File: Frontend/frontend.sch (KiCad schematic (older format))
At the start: 0 parts

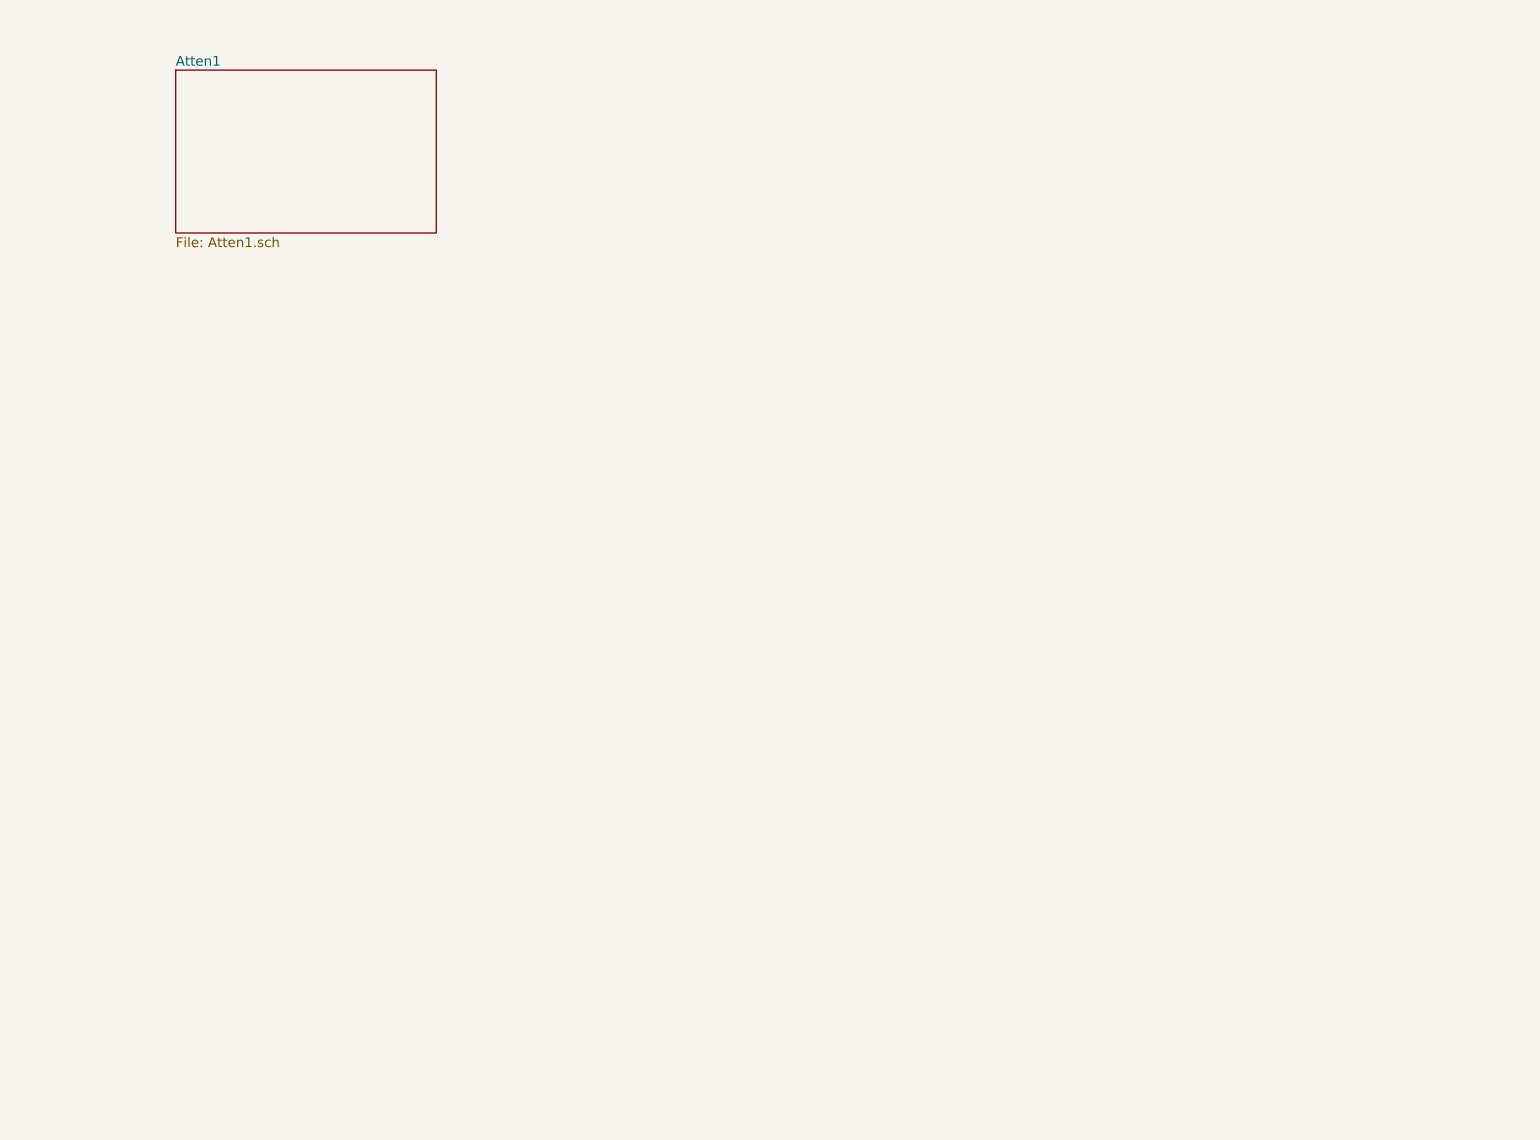
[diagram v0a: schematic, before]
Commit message: Frontend schematic ready to go to layout
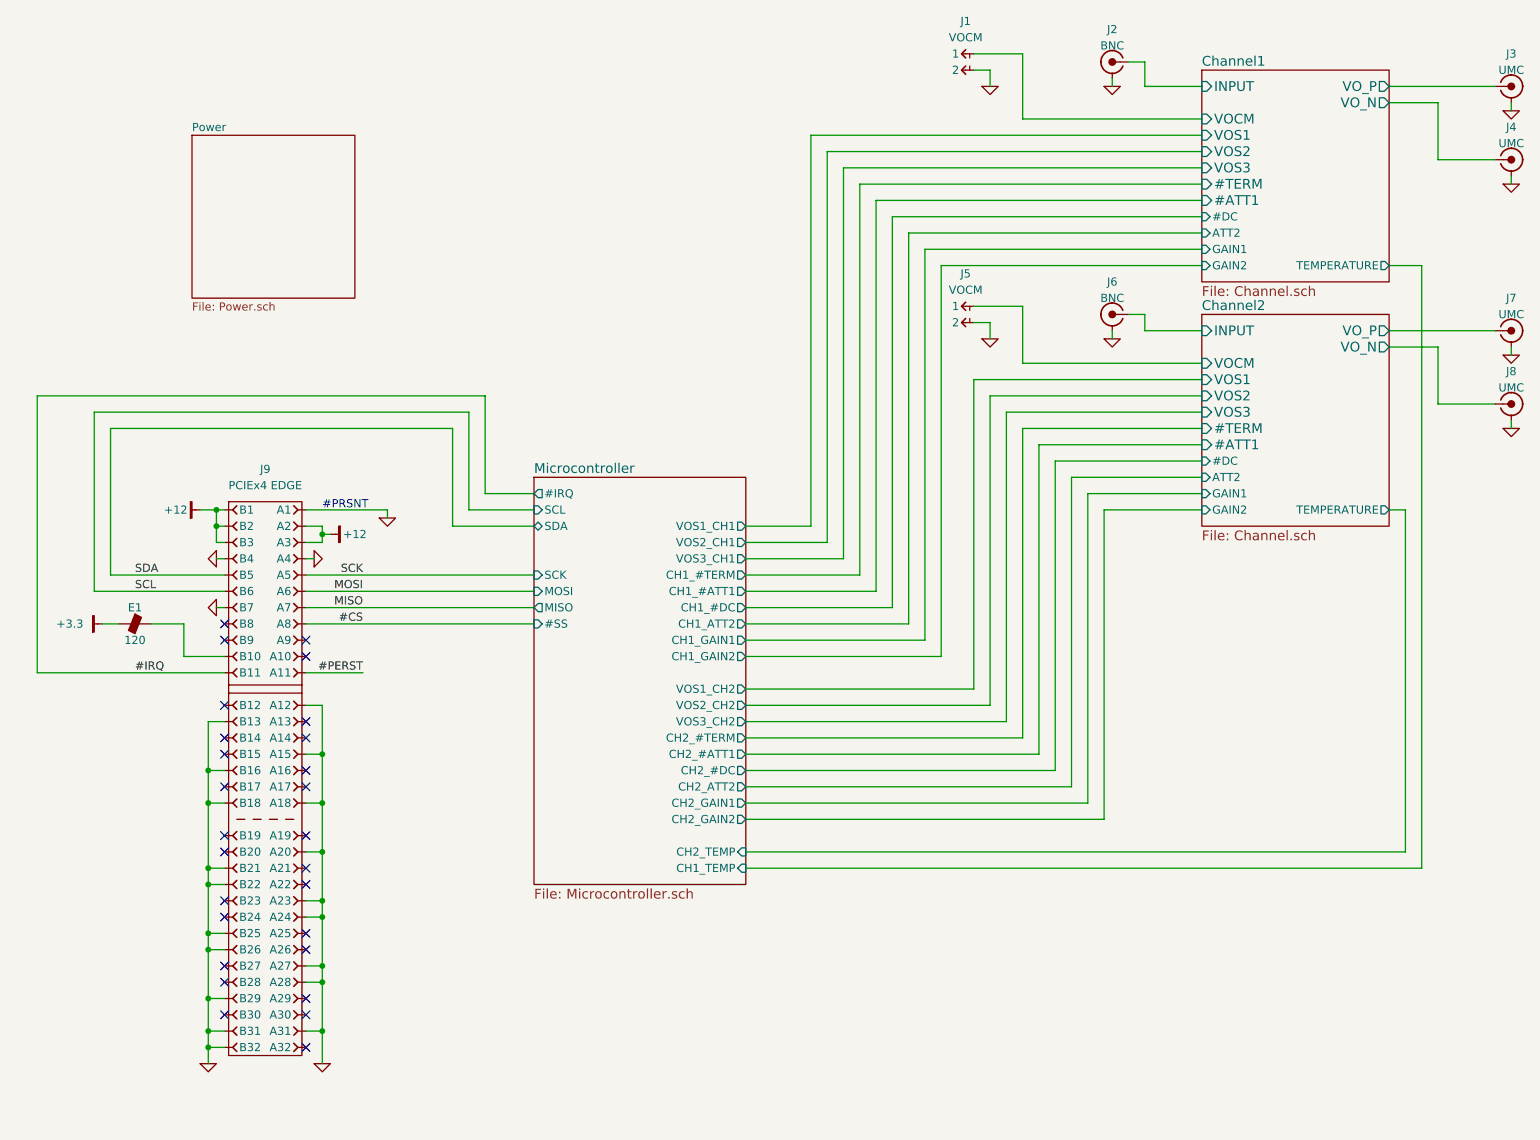
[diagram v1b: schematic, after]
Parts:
- added E1: 120, IPC7351-Nominal:RESC3216X60, symbol BEAD-1206
- added J1, J5: VOCM, conn-100mil:CONN-100MIL-M-1x2, symbol CONN-100MIL-M-1x2
- added J2, J6: BNC, manuf:CONN-BNC-1-1337543-0, symbol CONN-TE-1-1337543-0
- added J3, J4, J7, J8: UMC, conn-molex:CONN-MOLEX-0734120110, symbol CONN-MOLEX-0734120110
- added J9: PCIEx4 EDGE, conn-fci:CONN-10018784-10201TLF-PCIEx4-FCI, symbol CONN-10018784-10201TLF-PCIEx4
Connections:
- new net: E1.2, J9.B10
- new net #CS: J9.A8
- new net #IRQ: J9.B11
- new net #PERST: J9.A11
- new net +12: J9.A2, J9.A3, J9.B1, J9.B2, J9.B3
- new net +3.3: E1.1
- new net Channel1/INPUT: J2.1
- new net Channel1/VOCM: J1.1
- new net Channel1/VO_N: J4.1
- new net Channel1/VO_P: J3.1
- new net Channel2/INPUT: J6.1
- new net Channel2/VOCM: J5.1
- new net Channel2/VO_N: J8.1
- new net Channel2/VO_P: J7.1
- new net GND: J1.2, J2.2, J3.2, J4.2, J5.2, J6.2, J7.2, J8.2, J9.A1, J9.A12, J9.A15, J9.A18, J9.A20, J9.A23, J9.A24, J9.A27, J9.A28, J9.A31, J9.A4, J9.B13, J9.B16, J9.B18, J9.B21, J9.B22, J9.B25, J9.B26, J9.B29, J9.B31, J9.B32, J9.B4, J9.B7
- new net MISO: J9.A7
- new net MOSI: J9.A6
- new net SCK: J9.A5
- new net SCL: J9.B6
- new net SDA: J9.B5
- no-connect marks 0 -> 27
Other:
- note added: "#PRSNT"

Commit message: More layout work
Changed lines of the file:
@@
 F7 "CH2_#TERM" O R 5100 5300 50
 F8 "CH2_#ATT1" O R 5100 5400 50
-F9 "SDA" B L 3800 4000 50
-F10 "SCL" I L 3800 3900 50
+F9 "SDA" B L 3800 4200 50
+F10 "SCL" I L 3800 4100 50
 F11 "#SS" I L 3800 4600 50
-F12 "#IRQ" O L 3800 3800 50
+F12 "#IRQ" O L 3800 4000 50
 F13 "CH2_#DC" O R 5100 5500 50
 F14 "CH1_#DC" O R 5100 4500 50
@@
 F27 "CH1_TEMP" I R 5100 6100 50
 F28 "CH2_TEMP" I R 5100 6000 50
+F29 "TEMP_VRELAY" I L 3800 3800 50
+F30 "TEMP_V5" I L 3800 3900 50
 $EndSheet
 $Sheet
@@
 F0 "Power" 50
 F1 "Power.sch" 50
+F2 "TEMP_VRELAY" O R 2700 1700 50
+F3 "TEMP_V5" O R 2700 1800 50
 $EndSheet
 $Comp
@@
 Connection ~ 2500 5400
 Wire Wire Line
-	3800 4000 3300 4000
-Wire Wire Line
-	3300 4000 3300 3400
-Wire Wire Line
-	3300 3400 1200 3400
+	3800 4200 3000 4200
+Wire Wire Line
+	3000 4200 3000 3400
+Wire Wire Line
+	3000 3400 1200 3400
 Wire Wire Line
 	1200 3400 1200 4300
@@
 	1100 4400 1100 3300
 Wire Wire Line
-	1100 3300 3400 3300
-Wire Wire Line
-	3400 3300 3400 3900
-Wire Wire Line
-	3400 3900 3800 3900
+	1100 3300 3100 3300
+Wire Wire Line
+	3100 3300 3100 4100
+Wire Wire Line
+	3100 4100 3800 4100
 Wire Wire Line
 	1250 4600 1150 4600
@@
 	1650 4800 1900 4800
 Wire Wire Line
-	3800 3800 3500 3800
-Wire Wire Line
-	3500 3800 3500 3200
-Wire Wire Line
-	3500 3200 750  3200
+	3800 4000 3200 4000
+Wire Wire Line
+	3200 4000 3200 3200
+Wire Wire Line
+	3200 3200 750  3200
 Wire Wire Line
 	750  3200 750  4900
@@
 Wire Wire Line
 	9250 2400 9050 2400
+Wire Wire Line
+	3800 3900 3400 3900
+Wire Wire Line
+	3400 3900 3400 1800
+Wire Wire Line
+	3400 1800 2700 1800
+Wire Wire Line
+	2700 1700 3500 1700
+Wire Wire Line
+	3500 1700 3500 3800
+Wire Wire Line
+	3500 3800 3800 3800
 $EndSCHEMATC

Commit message: Schematic touchups
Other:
- moved on the sheet: E1

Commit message: Route #IRQ and #PERST
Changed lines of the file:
@@
 LIBS:Altera
 LIBS:conn-te
+LIBS:Vishay
+LIBS:semi-trans-OnSemi
 LIBS:frontend-cache
 EELAYER 25 0
@@
 F29 "TEMP_VRELAY" I L 3800 3800 50
 F30 "TEMP_V5" I L 3800 3900 50
+F31 "#PERST" I L 3800 4900 50
 $EndSheet
 $Sheet
@@
 	2400 4600 3800 4600
 Wire Wire Line
-	2750 4900 2400 4900
+	2400 4900 3800 4900
 Wire Wire Line
 	1900 5200 1800 5200

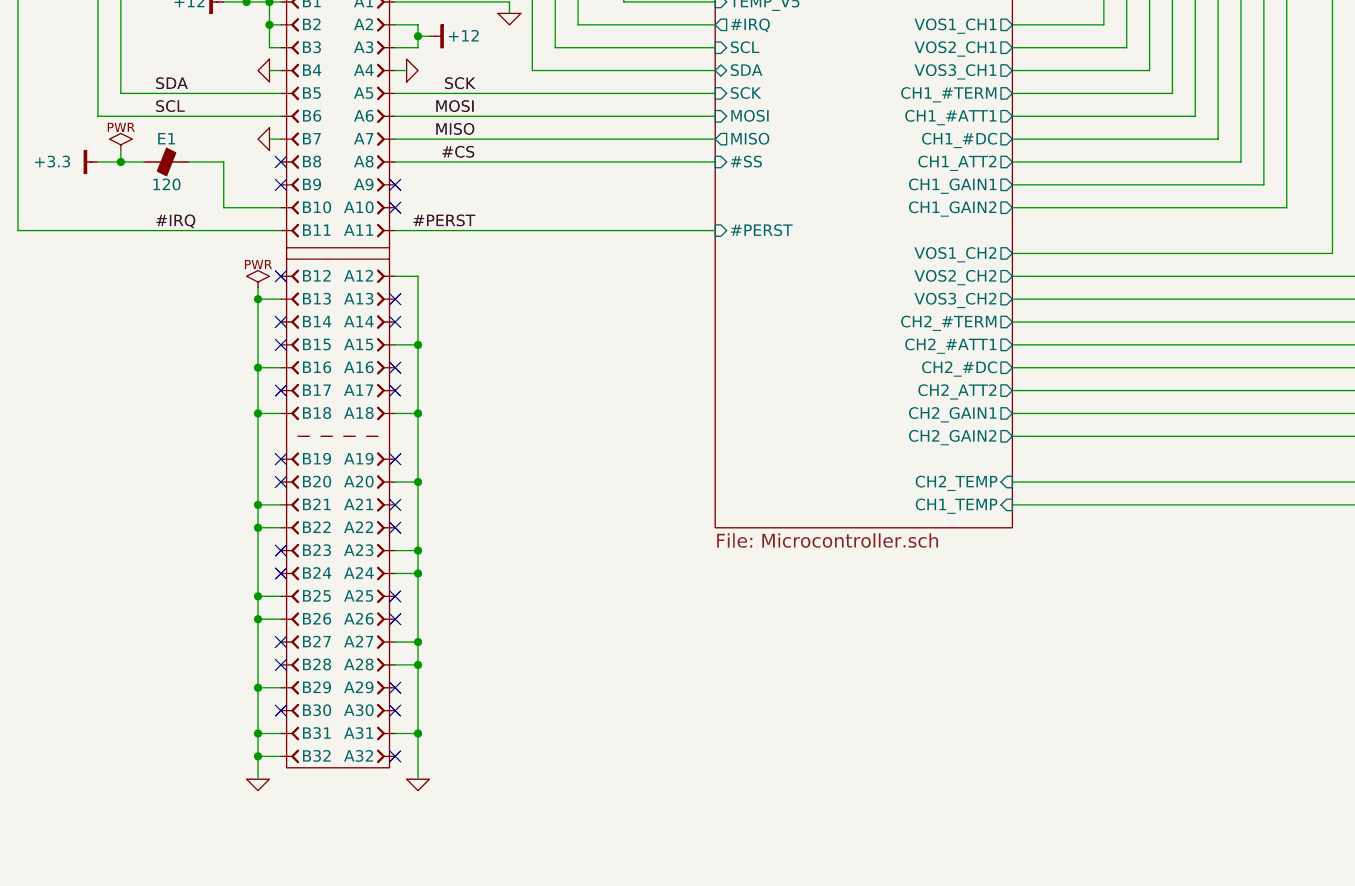
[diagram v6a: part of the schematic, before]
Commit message: Add testpoints
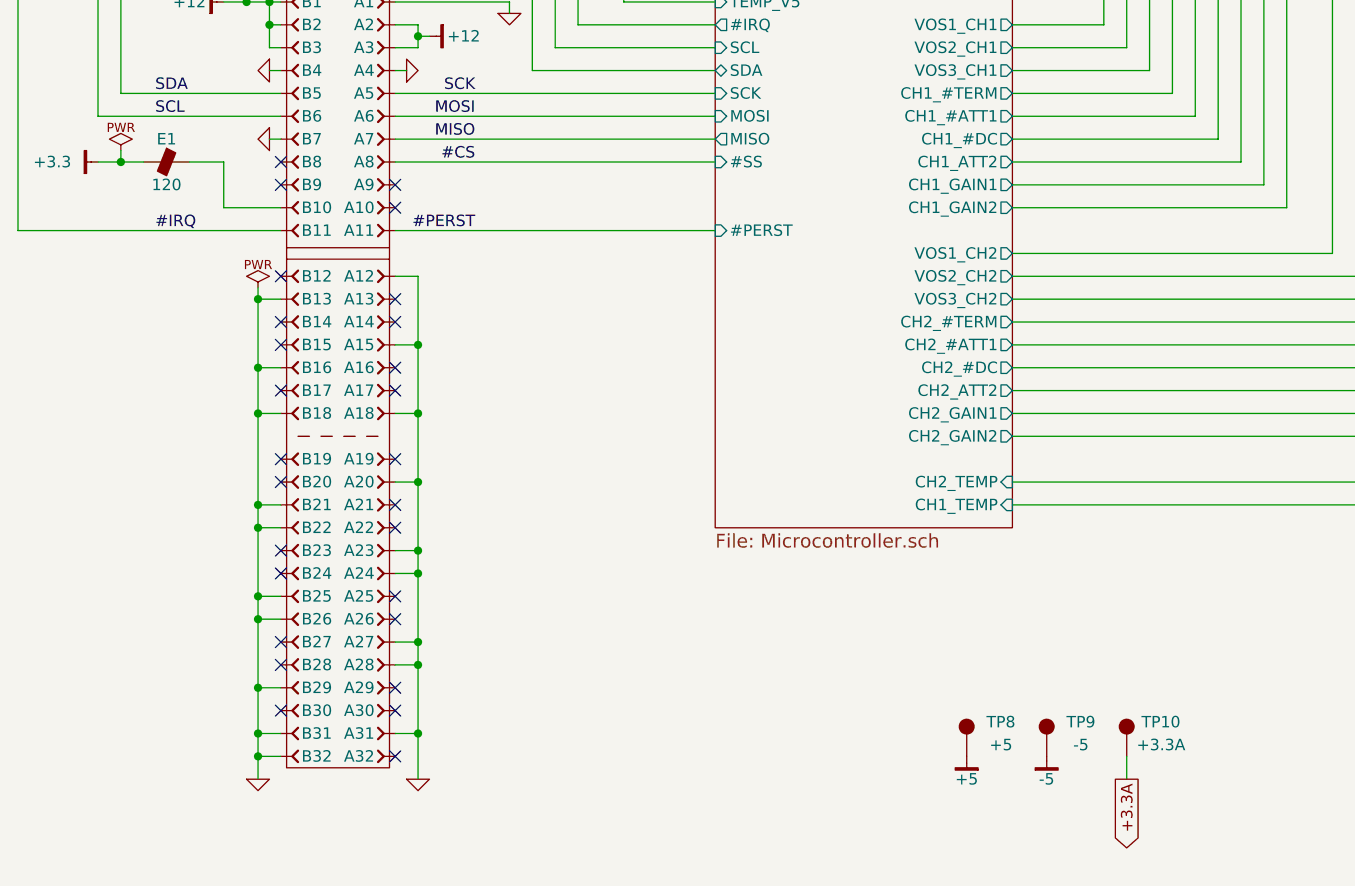
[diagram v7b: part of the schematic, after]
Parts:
- added TP10: +3.3A, conn-test:TEST-SMD-SMALL, symbol TESTPOINT
- added TP8: +5, conn-test:TEST-SMD-SMALL, symbol TESTPOINT
- added TP9: -5, conn-test:TEST-SMD-SMALL, symbol TESTPOINT
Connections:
- new net +3.3A: TP10.1
- new net +5: TP8.1
- new net -5: TP9.1
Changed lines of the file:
@@
 	3100 4100 3800 4100
 Wire Wire Line
-	1300 4600 1100 4600
+	1100 4600 1300 4600
 Wire Wire Line
 	1500 4600 1650 4600
@@
 $EndComp
 Connection ~ 1800 5200
+$Comp
+L TESTPOINT TP8
+U 1 1 5558DEAC
+P 4900 7200
+F 0 "TP8" H 5050 7350 50  0000 C CNN
+F 1 "+5" H 5050 7250 50  0000 C CNN
+F 2 "conn-test:TEST-SMD-SMALL" H 4900 7200 50  0001 C CNN
+F 3 "" H 4900 7200 50  0000 C CNN
+	1    4900 7200
+	1    0    0    -1
+$EndComp
+$Comp
+L +5 #PWR021
+U 1 1 5558E053
+P 4900 7200
+F 0 "#PWR021" H 4900 7250 30  0001 C CNN
+F 1 "+5" H 4900 7300 50  0000 C CNN
+F 2 "" H 4900 7200 60  0000 C CNN
+F 3 "" H 4900 7200 60  0000 C CNN
+	1    4900 7200
+	-1   0    0    1
+$EndComp
+$Comp
+L TESTPOINT TP9
+U 1 1 5558E378
+P 5250 7200
+F 0 "TP9" H 5400 7350 50  0000 C CNN
+F 1 "-5" H 5400 7250 50  0000 C CNN
+F 2 "conn-test:TEST-SMD-SMALL" H 5250 7200 50  0001 C CNN
+F 3 "" H 5250 7200 50  0000 C CNN
+	1    5250 7200
+	1    0    0    -1
+$EndComp
+$Comp
+L -5 #PWR022
+U 1 1 5558E5C7
+P 5250 7200
+F 0 "#PWR022" H 5250 7150 30  0001 C CNN
+F 1 "-5" H 5250 7100 50  0000 C CNN
+F 2 "" H 5250 7200 60  0000 C CNN
+F 3 "" H 5250 7200 60  0000 C CNN
+	1    5250 7200
+	1    0    0    -1
+$EndComp
+$Comp
+L TESTPOINT TP10
+U 1 1 5558E8F0
+P 5600 7200
+F 0 "TP10" H 5750 7350 50  0000 C CNN
+F 1 "+3.3A" H 5750 7250 50  0000 C CNN
+F 2 "conn-test:TEST-SMD-SMALL" H 5600 7200 50  0001 C CNN
+F 3 "" H 5600 7200 50  0000 C CNN
+	1    5600 7200
+	1    0    0    -1
+$EndComp
+Text GLabel 5600 7300 3    50   Output ~ 0
++3.3A
+Wire Wire Line
+	5600 7300 5600 7200
 $EndSCHEMATC

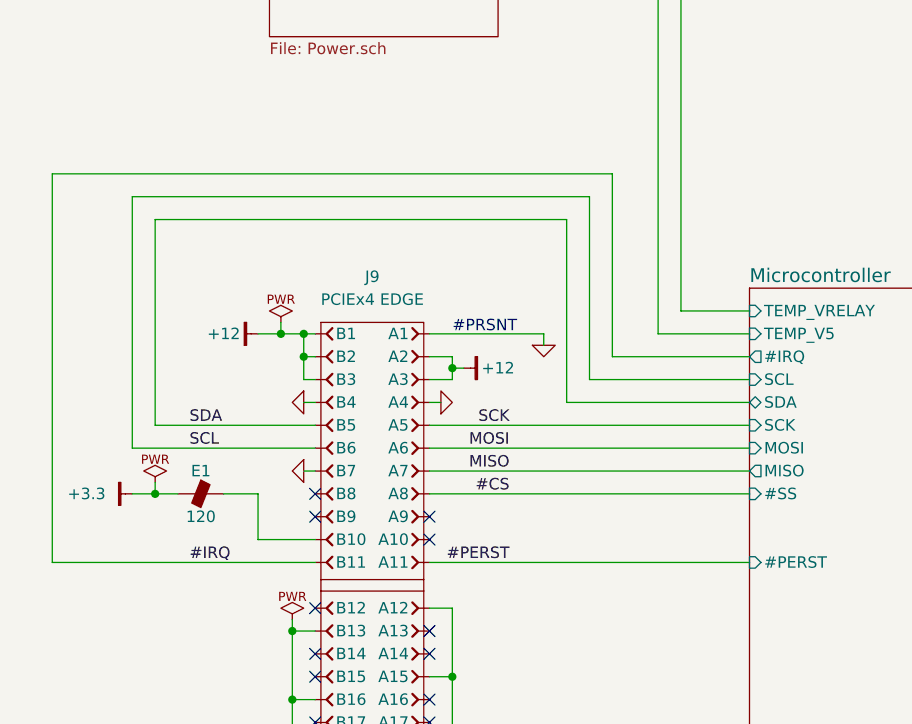
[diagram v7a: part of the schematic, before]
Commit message: Digital decoupling/termination tweaks
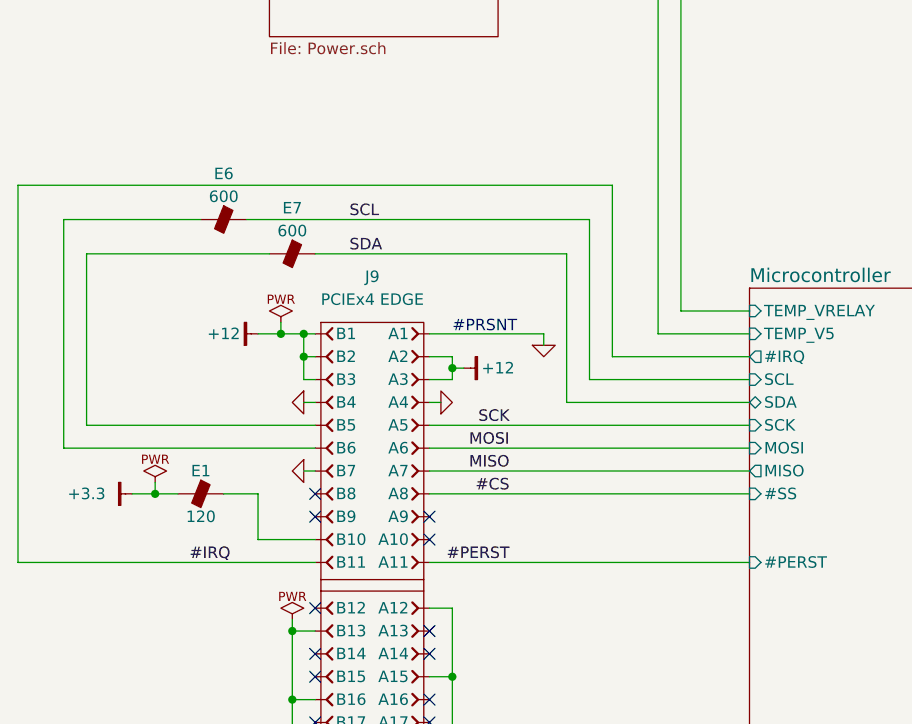
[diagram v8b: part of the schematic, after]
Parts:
- added E6, E7: 600, IPC7351-Nominal:INDC1005X60, symbol BEAD-0402
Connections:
- net SCL: now also E6.2; no longer J9.B6
- net SDA: now also E7.2; no longer J9.B5
- new net: E7.1, J9.B5
- new net: E6.1, J9.B6
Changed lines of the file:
@@
 	0    1    1    0
 $EndComp
-Text Label 1350 4400 0    50   ~ 0
+Text Label 2050 3400 0    50   ~ 0
 SCL
-Text Label 1350 4300 0    50   ~ 0
+Text Label 2050 3550 0    50   ~ 0
 SDA
 $Comp
@@
 	2450 4200 2400 4200
 Wire Wire Line
-	750  4900 1900 4900
+	600  4900 1900 4900
 Wire Wire Line
 	1850 4500 1900 4500
 Wire Wire Line
-	1100 4400 1900 4400
-Wire Wire Line
-	1200 4300 1900 4300
+	800  4400 1900 4400
+Wire Wire Line
+	900  4300 1900 4300
 Wire Wire Line
 	1850 4200 1900 4200
@@
 Connection ~ 2500 5400
 Wire Wire Line
-	3800 4200 3000 4200
-Wire Wire Line
-	3000 4200 3000 3400
-Wire Wire Line
-	3000 3400 1200 3400
-Wire Wire Line
-	1200 3400 1200 4300
-Wire Wire Line
-	1100 4400 1100 3300
-Wire Wire Line
-	1100 3300 3100 3300
-Wire Wire Line
-	3100 3300 3100 4100
+	3000 4200 3800 4200
+Wire Wire Line
+	3000 3550 3000 4200
+Wire Wire Line
+	900  3550 900  4300
+Wire Wire Line
+	800  4400 800  3400
+Wire Wire Line
+	3100 3400 3100 4100
 Wire Wire Line
 	3100 4100 3800 4100
@@
 	3800 4000 3200 4000
 Wire Wire Line
-	3200 4000 3200 3200
-Wire Wire Line
-	3200 3200 750  3200
-Wire Wire Line
-	750  3200 750  4900
+	3200 4000 3200 3250
+Wire Wire Line
+	3200 3250 600  3250
+Wire Wire Line
+	600  3250 600  4900
 Wire Wire Line
 	7450 1150 7550 1150
@@
 Wire Wire Line
 	5600 7300 5600 7200
+$Comp
+L BEAD-0402 E?
+U 1 1 555A74A2
+P 1500 3400
+AR Path="/552B011F/555A74A2" Ref="E?"  Part="1"
+AR Path="/555A74A2" Ref="E6"  Part="1"
+F 0 "E6" H 1500 3600 50  0000 C CNN
+F 1 "600" H 1500 3500 50  0000 C CNN
+F 2 "IPC7351-Nominal:INDC1005X60" H 1500 3400 50  0001 C CNN
+F 3 "" H 1500 3450 60  0000 C CNN
+F 4 "PE-0402FB601ST" H 1500 3400 60  0001 C CNN "PN"
+F 5 "Pulse" H 1500 3400 60  0001 C CNN "Manuf"
+F 6 "DIST DIGIKEY 553-2374-1-ND" H 1500 3400 60  0001 C CNN "BOM"
+	1    1500 3400
+	1    0    0    -1
+$EndComp
+$Comp
+L BEAD-0402 E?
+U 1 1 555A757C
+P 1800 3550
+AR Path="/552B011F/555A757C" Ref="E?"  Part="1"
+AR Path="/555A757C" Ref="E7"  Part="1"
+F 0 "E7" H 1800 3750 50  0000 C CNN
+F 1 "600" H 1800 3650 50  0000 C CNN
+F 2 "IPC7351-Nominal:INDC1005X60" H 1800 3550 50  0001 C CNN
+F 3 "" H 1800 3600 60  0000 C CNN
+F 4 "PE-0402FB601ST" H 1800 3550 60  0001 C CNN "PN"
+F 5 "Pulse" H 1800 3550 60  0001 C CNN "Manuf"
+F 6 "DIST DIGIKEY 553-2374-1-ND" H 1800 3550 60  0001 C CNN "BOM"
+	1    1800 3550
+	1    0    0    -1
+$EndComp
+Wire Wire Line
+	800  3400 1400 3400
+Wire Wire Line
+	1600 3400 3100 3400
+Wire Wire Line
+	3000 3550 1900 3550
+Wire Wire Line
+	1700 3550 900  3550
 $EndSCHEMATC
